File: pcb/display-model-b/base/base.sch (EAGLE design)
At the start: 37 parts, among them J1 SNG-2MM-HEADER-07-V, Q1 MMBT3904, Q2 MMBT3904, Q3 MMBT3904, Q4 MMBT3904, U1 PCA9634PW, U2 TSL2561FN, X1 CLOCK_LED_SEGMENT, X2 CLOCK_LED_SEGMENT, X3 CLOCK_LED_SEGMENT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

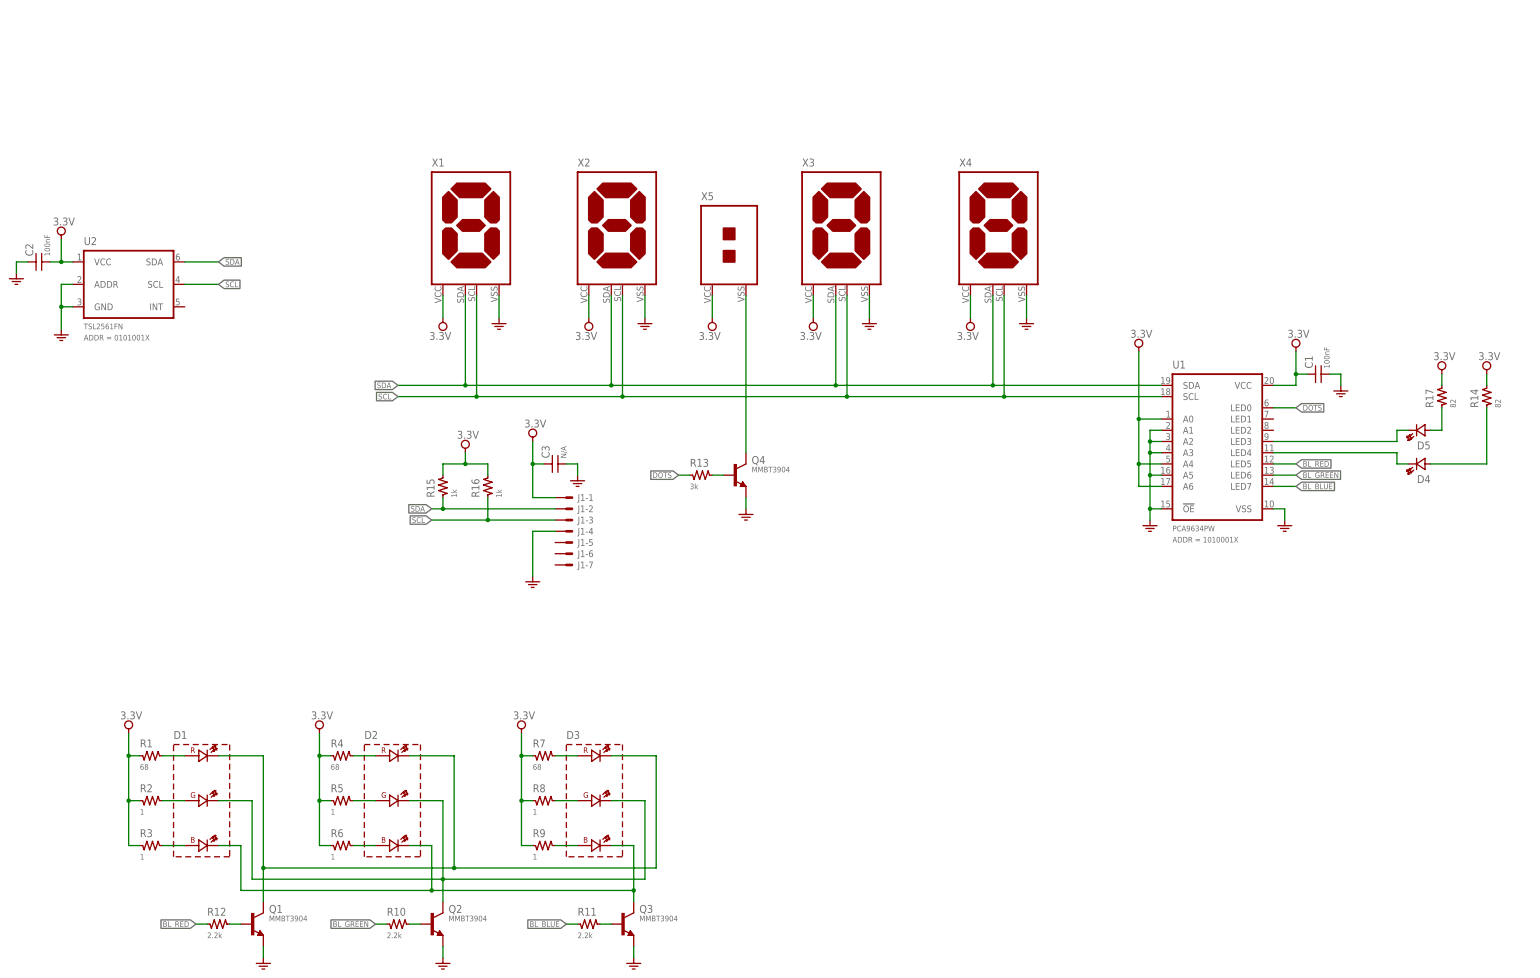
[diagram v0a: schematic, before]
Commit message: Corrected drawings of touch panel PCB
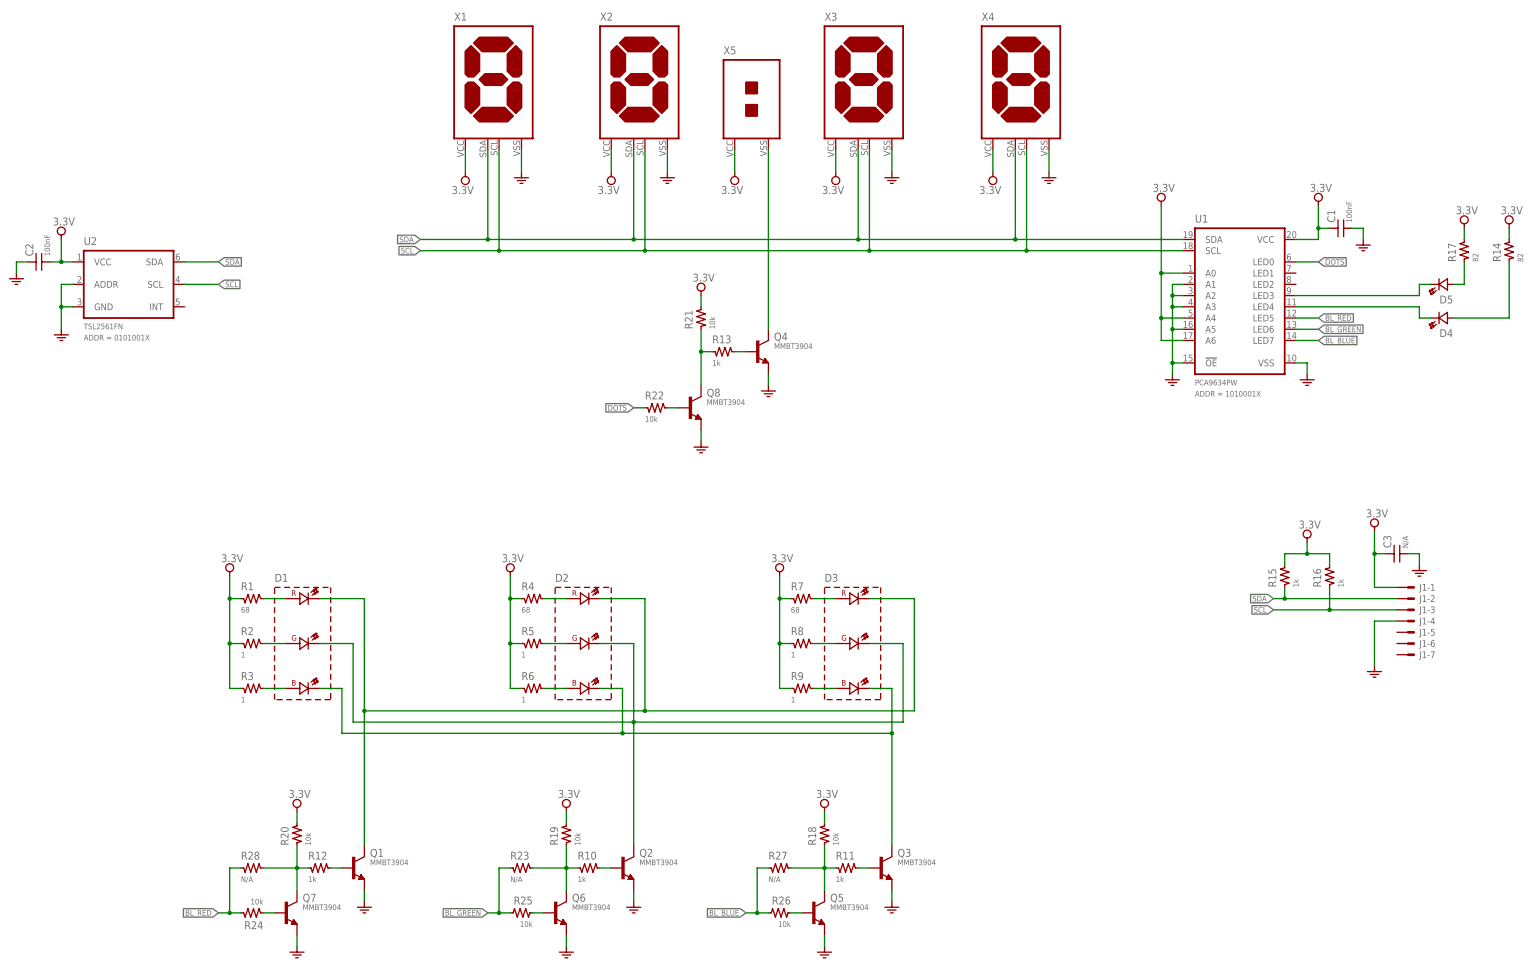
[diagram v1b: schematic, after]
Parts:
- added Q5, Q6, Q7, Q8: MMBT3904, Transistor:MMBT3904
- added R18, R19, R20, R21, R22, R24, R25, R26: 10k, Passive:RES-0603
- added R23, R27, R28: N/A, Passive:RES-0603
- R10, R11, R12: value 2.2k -> 1k
- R13: value 3k -> 1k
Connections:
- new net N$22: Q6.C, R10.1, R19.1, R23.2
- new net N$23: Q5.C, R11.1, R18.1, R27.2
- new net N$24: Q7.C, R12.1, R20.1, R28.2
- new net N$25: Q5.B, R26.1
- new net N$26: Q8.C, R13.1, R21.1
- new net N$27: Q8.B, R22.2
- new net N$28: Q6.B, R25.1
- new net N$30: Q7.B, R24.1
- net 3.3V: now also R18.2, R19.2, R20.2, R21.2
- net BL_BLUE: now also R26.2, R27.1; no longer R11.1
- net BL_GREEN: now also R23.1, R25.2; no longer R10.1
- net BL_RED: now also R24.2, R28.1; no longer R12.1
- net DOTS: now also R22.1; no longer R13.1
- net GND: now also Q5.E, Q6.E, Q7.E, Q8.E
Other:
- moved on the sheet: C1, C3, D1, D2, D3, D4, D5, J1-1, J1-2, J1-3, J1-4, J1-5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
